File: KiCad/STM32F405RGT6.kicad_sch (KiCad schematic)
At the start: 44 parts, among them IC1 FT232RQ-REEL, J1 USB_C_Receptacle_USB2.0, J2 USB_C_Receptacle_USB2.0, SW1 SW_SPST, U1 STM32F405RGTx, U2 AT24CS64-SSHM, Y1 25MHz

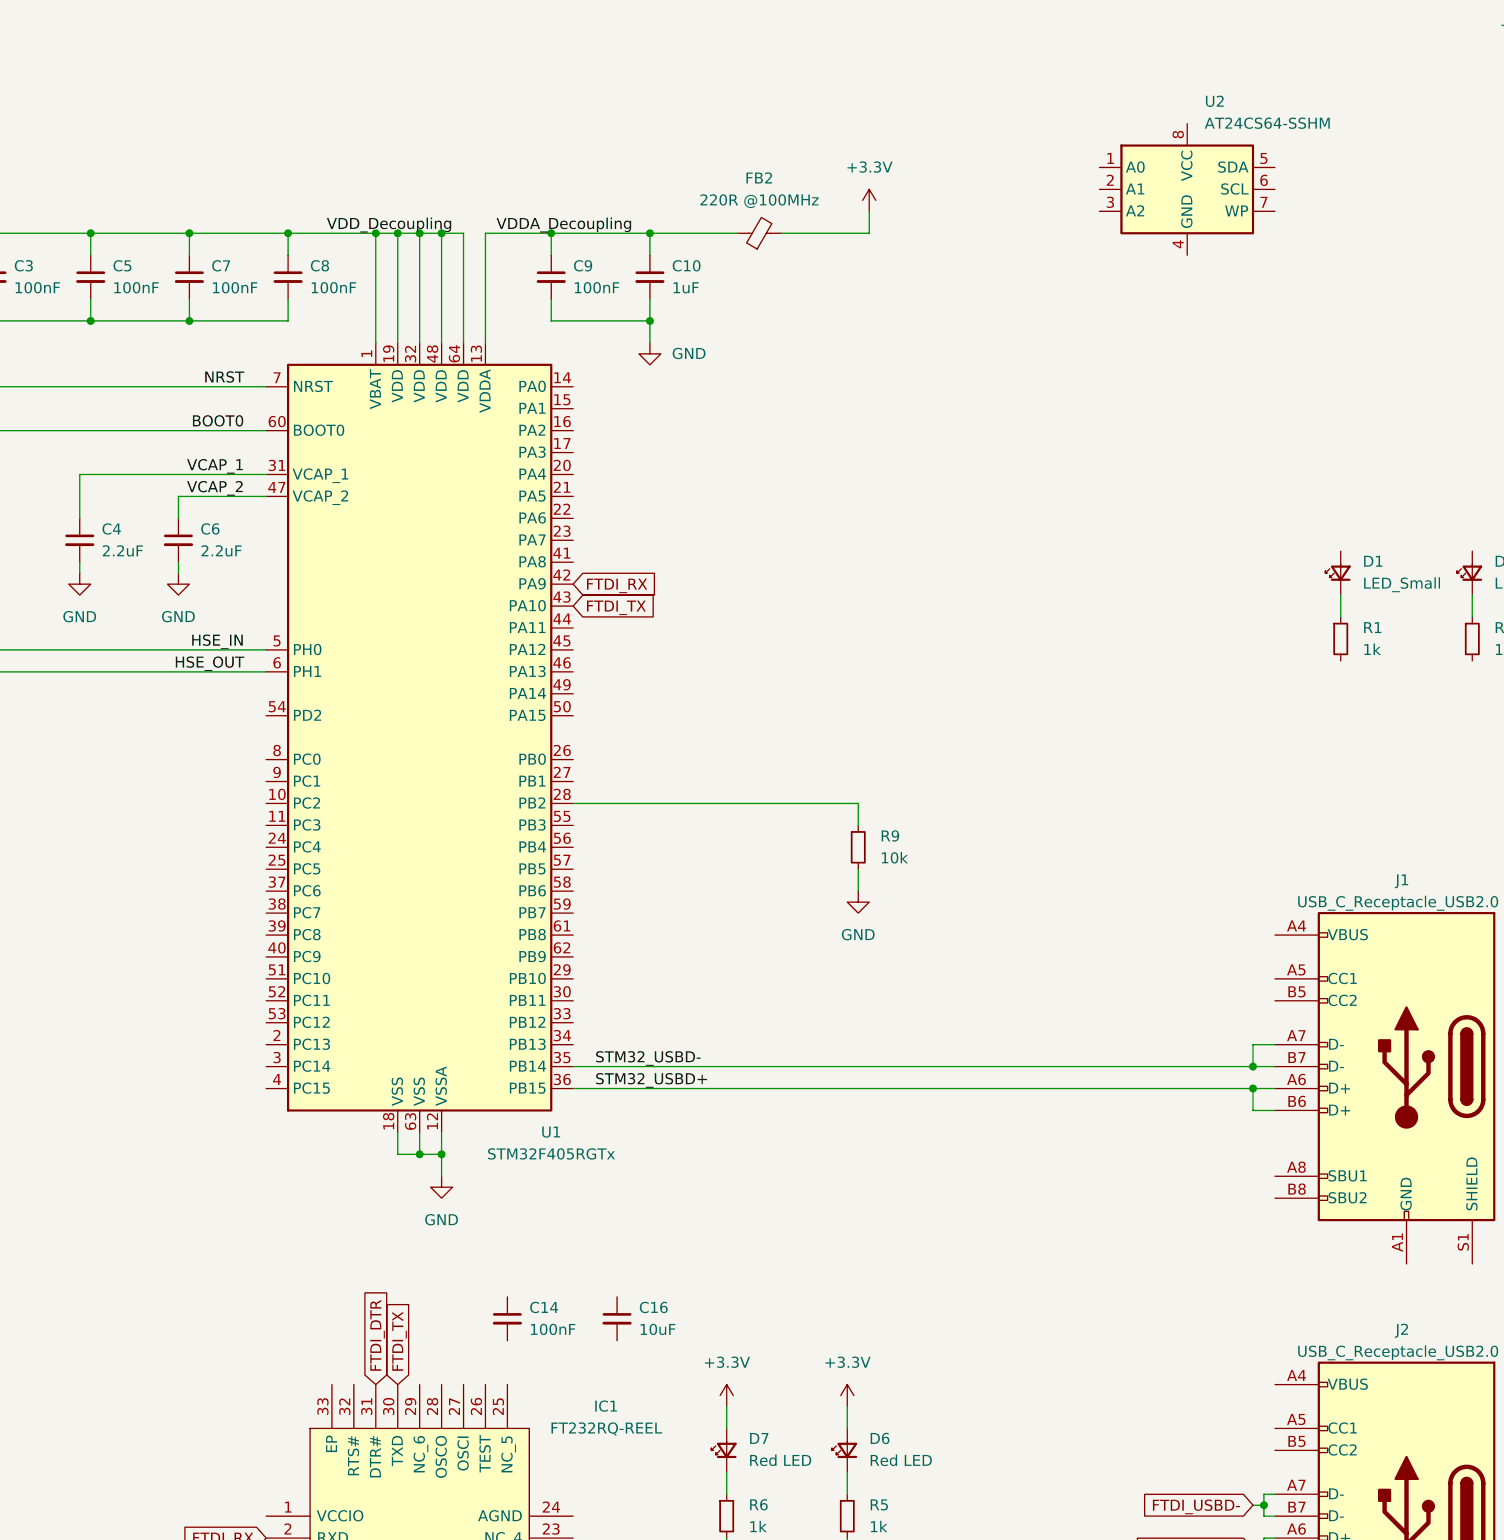
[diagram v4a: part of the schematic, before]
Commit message: Updated STM32 Cube and KiCad files
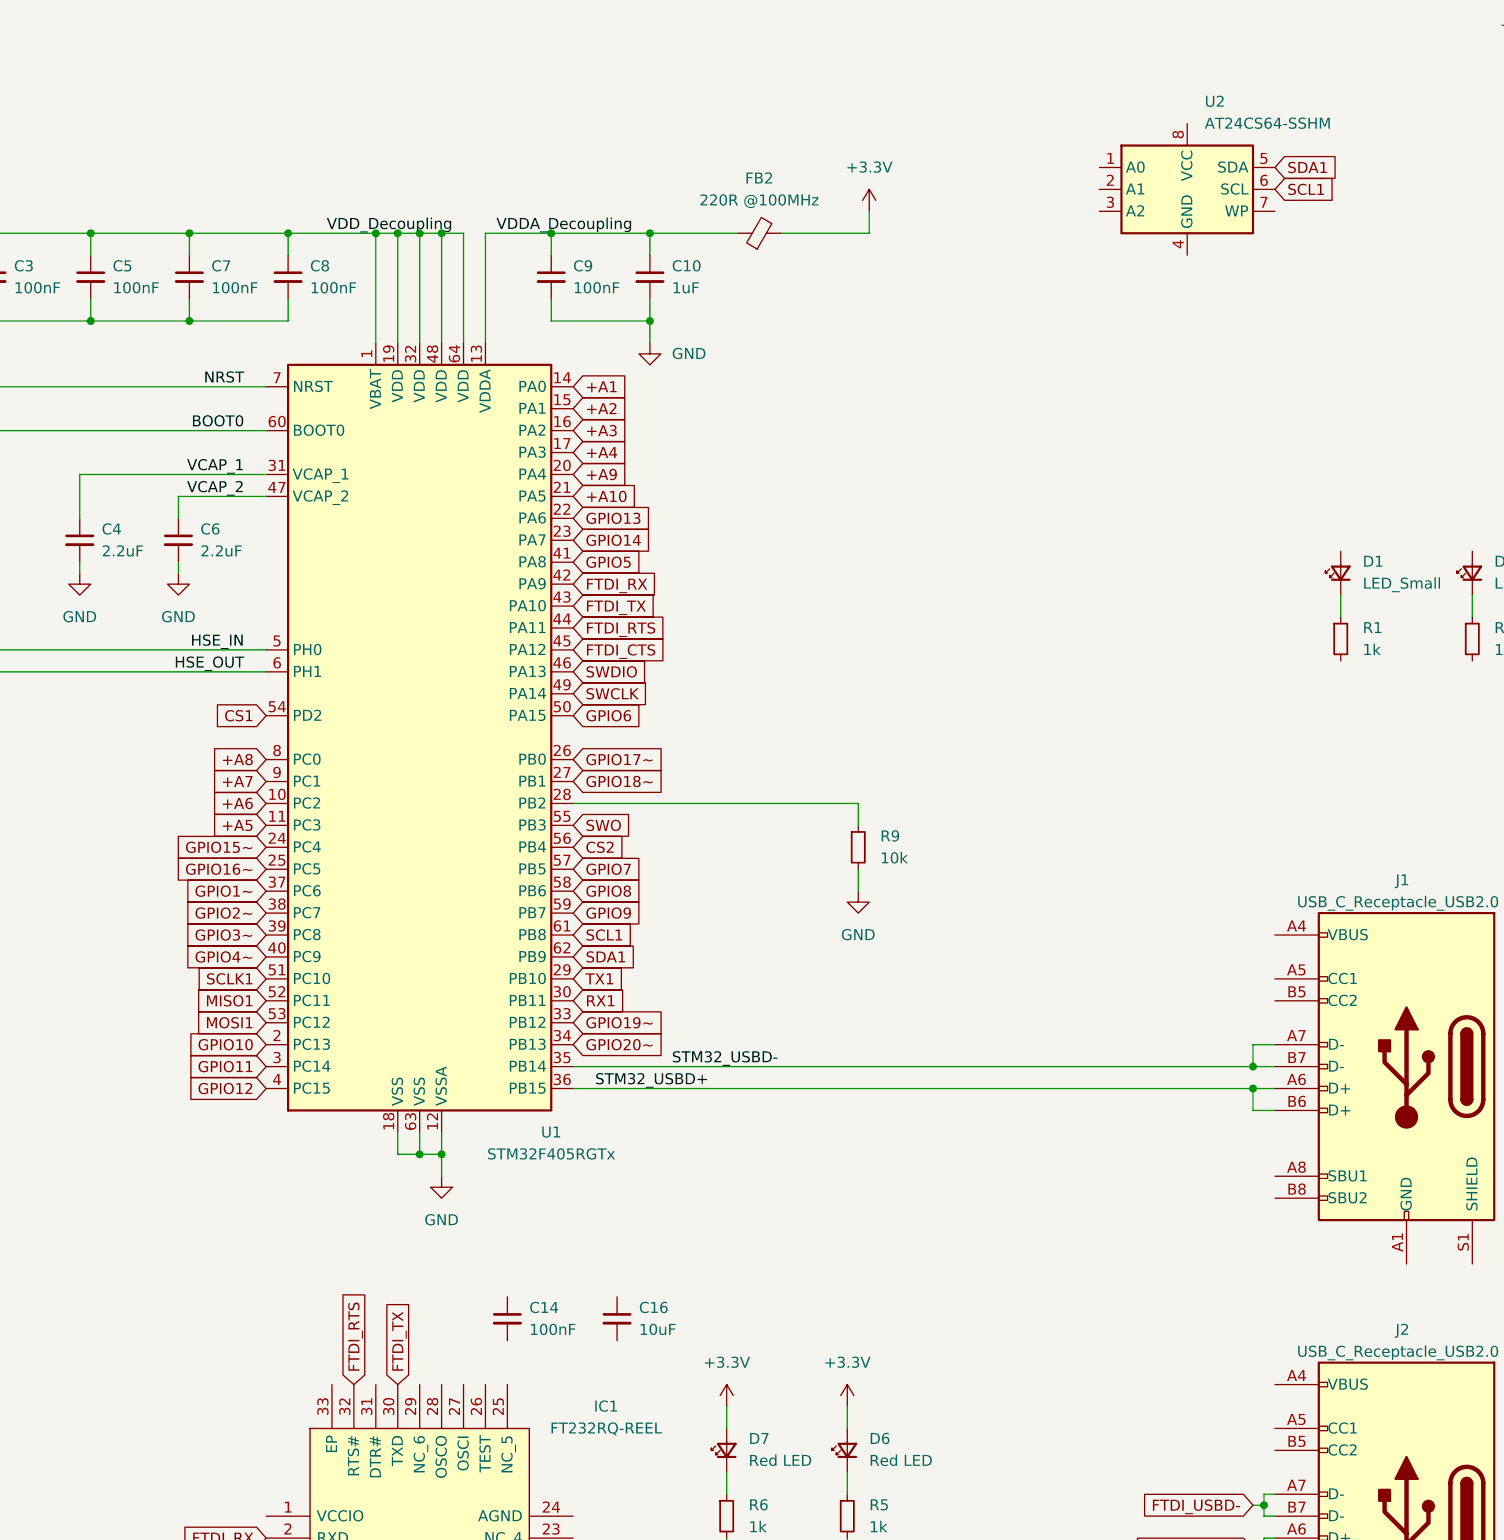
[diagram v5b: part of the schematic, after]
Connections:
- net FTDI_CTS: now also U1.45 (PA12)
- net FTDI_RTS: now reaches IC1.32 (RTS#)
- net FTDI_RTS: now also U1.44 (PA11)
- net +A6: now reaches U1.10 (PC2)
- net +A5: now reaches U1.11 (PC3)
- net +A1: now reaches U1.14 (PA0)
- net +A2: now reaches U1.15 (PA1)
- net +A3: now reaches U1.16 (PA2)
- net +A4: now reaches U1.17 (PA3)
- net GPIO10: now reaches U1.2 (PC13)
- net +A9: now reaches U1.20 (PA4)
- net +A10: now reaches U1.21 (PA5)
- net GPIO13: now reaches U1.22 (PA6)
- net GPIO14: now reaches U1.23 (PA7)
- net GPIO15~: now reaches U1.24 (PC4)
- net GPIO16~: now reaches U1.25 (PC5)
- net GPIO17~: now reaches U1.26 (PB0)
- net GPIO18~: now reaches U1.27 (PB1)
- net TX1: now reaches U1.29 (PB10)
- net GPIO11: now reaches U1.3 (PC14)
- net RX1: now reaches U1.30 (PB11)
- net GPIO19~: now reaches U1.33 (PB12)
- net GPIO20~: now reaches U1.34 (PB13)
- net GPIO1~: now reaches U1.37 (PC6)
- net GPIO2~: now reaches U1.38 (PC7)
- net GPIO3~: now reaches U1.39 (PC8)
- net GPIO12: now reaches U1.4 (PC15)
- net GPIO4~: now reaches U1.40 (PC9)
- net GPIO5: now reaches U1.41 (PA8)
- net SWDIO: now reaches U1.46 (PA13)
- net SWCLK: now reaches U1.49 (PA14)
- net GPIO6: now reaches U1.50 (PA15)
- net SCLK1: now reaches U1.51 (PC10)
- net MISO1: now reaches U1.52 (PC11)
- net MOSI1: now reaches U1.53 (PC12)
- net CS1: now reaches U1.54 (PD2)
- net SWO: now reaches U1.55 (PB3)
- net CS2: now reaches U1.56 (PB4)
- net GPIO7: now reaches U1.57 (PB5)
- net GPIO8: now reaches U1.58 (PB6)
- net GPIO9: now reaches U1.59 (PB7)
- net SCL1: now reaches U1.61 (PB8)
- net SCL1: now also U2.6 (SCL)
- net SDA1: now reaches U1.62 (PB9)
- net SDA1: now also U2.5 (SDA)
- net +A8: now reaches U1.8 (PC0)
- net +A7: now reaches U1.9 (PC1)
- net FTDI_DTR: no longer names the net of IC1.31 (DTR#)

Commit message: Update Schematic and PCB
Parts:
- added D10, D9: PRTR5V0U2X, Package_TO_SOT_SMD:SOT-143, symbol Power_Protection:PRTR5V0U2X
- added FB3, FB4: 220R @100MHz, Inductor_SMD:L_0603_1608Metric, symbol Device:FerriteBead_Small
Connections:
- net FTDI_USBD+: now also D9.3 (I/O2)
- net FTDI_USBD-: now also D9.2 (I/O1)
- net GND: now also J1.A1 (GND), J1.A12 (GND), J1.B1 (GND), J1.B12 (GND), J2.A1 (GND), J2.A12 (GND), J2.B1 (GND), J2.B12 (GND), D10.1 (GND), D9.1 (GND)
- net STM32_USBD+: now also D10.3 (I/O2)
- net STM32_USBD-: now also D10.2 (I/O1)
- net at J1.A4 (VBUS), J1.A9 (VBUS), J1.B4 (VBUS)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: now also D10.4 (VCC), FB3.2
- net at J2.A4 (VBUS), J2.A9 (VBUS), J2.B4 (VBUS)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: now also D9.4 (VCC), FB4.2
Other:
- moved on the sheet: D1, D2, D3, D5, J2, R1, R2, R3, R4

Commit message: Updated PCB and Schematic
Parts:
- removed C14, C15: 100nF, Capacitor_SMD:C_0603_1608Metric, symbol Device:C_Small
- removed C16: 10uF, Capacitor_SMD:C_0603_1608Metric, symbol Device:C_Small
- removed D6, D7: Red LED, LED_SMD:LED_0603_1608Metric, symbol Device:LED_Small
- removed D9: PRTR5V0U2X, Package_TO_SOT_SMD:SOT-143, symbol Power_Protection:PRTR5V0U2X
- removed FB4: 220R @100MHz, Inductor_SMD:L_0603_1608Metric, symbol Device:FerriteBead_Small
- removed IC1: FT232RQ-REEL, Package_DFN_QFN:QFN-32-1EP_5x5mm_P0.5mm_EP3.3x3.3mm_ThermalVias, symbol FT232RQ-REEL:FT232RQ-REEL
- removed J2: USB_C_Receptacle_USB2.0, Connector_USB:USB_C_Receptacle_HRO_TYPE-C-31-M-12, symbol Connector:USB_C_Receptacle_USB2.0
- removed R5, R6: 1k, Resistor_SMD:R_0603_1608Metric, symbol Device:R_Small
- added D6: D_Small, symbol Device:D_Small
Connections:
- net +5V: now also D6.1 (K)
- net USB_5V: now reaches D10.4 (VCC), FB3.2, J1.A4 (VBUS), J1.A9 (VBUS), J1.B4 (VBUS), J1.B9 (VBUS)
- net at FB3.1: now also D6.2 (A)
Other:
- note added: "90 Ohm differential pair for USB PCB Type: Trace Width: Trace Spacing: 1.6 mm, 4 layer board"
- moved on the sheet: D10, FB3, J1

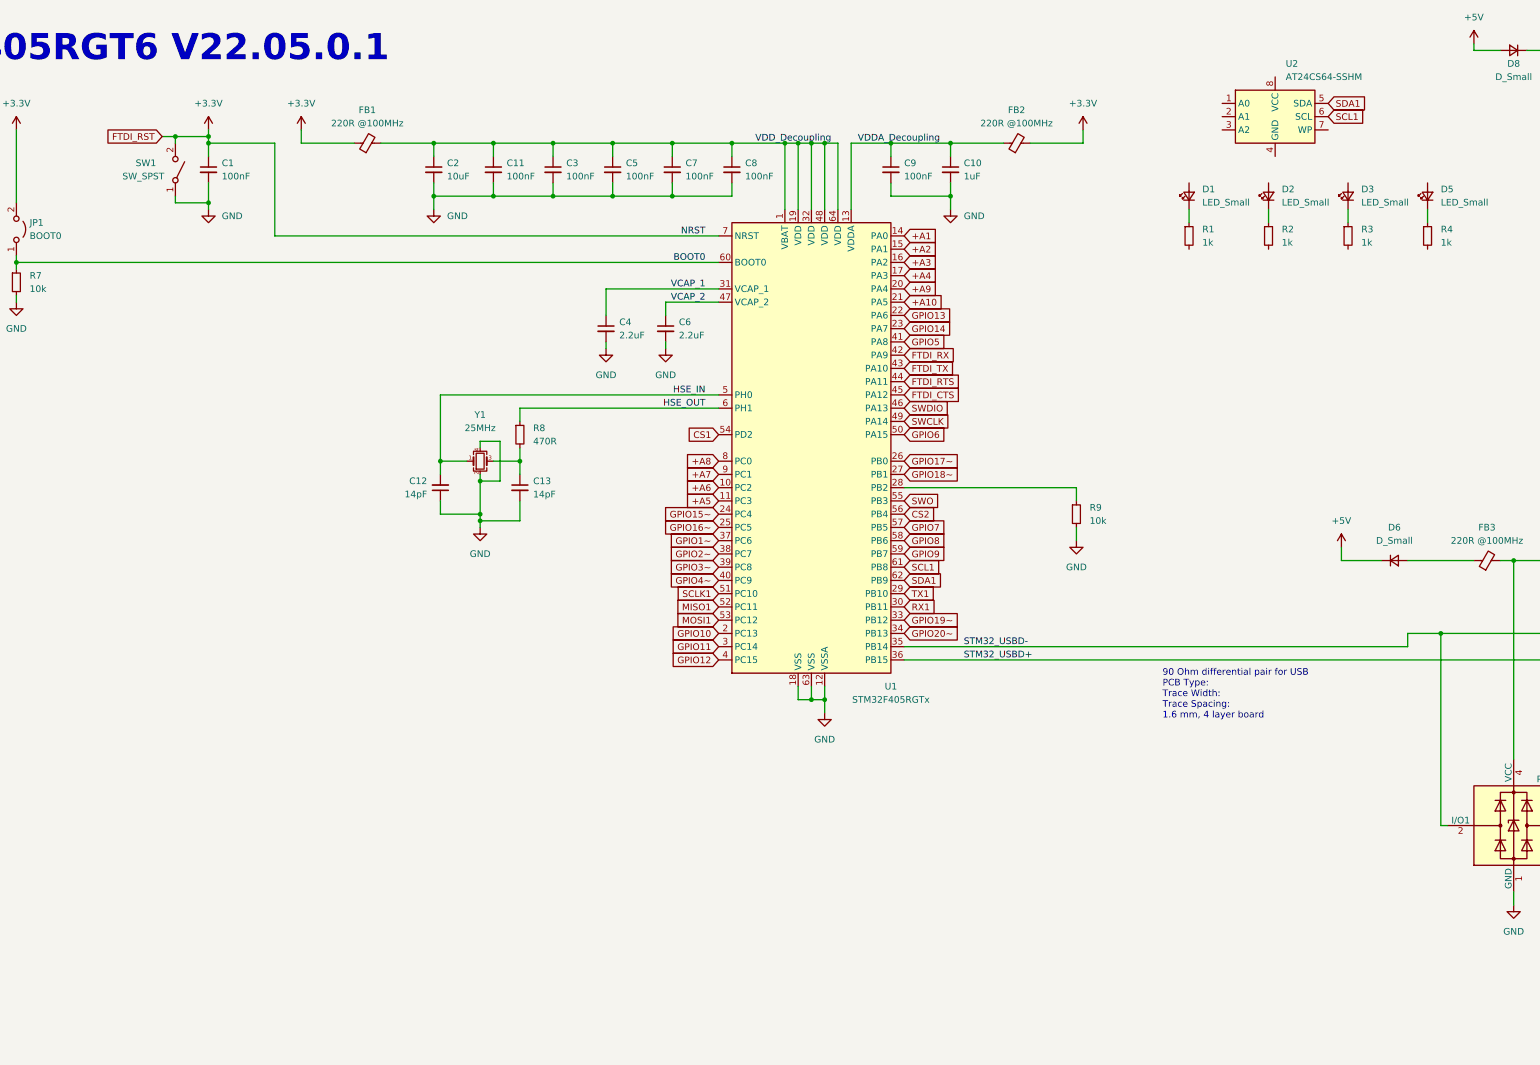
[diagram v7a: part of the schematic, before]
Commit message: Removed FTDI chip and rearranged pinout
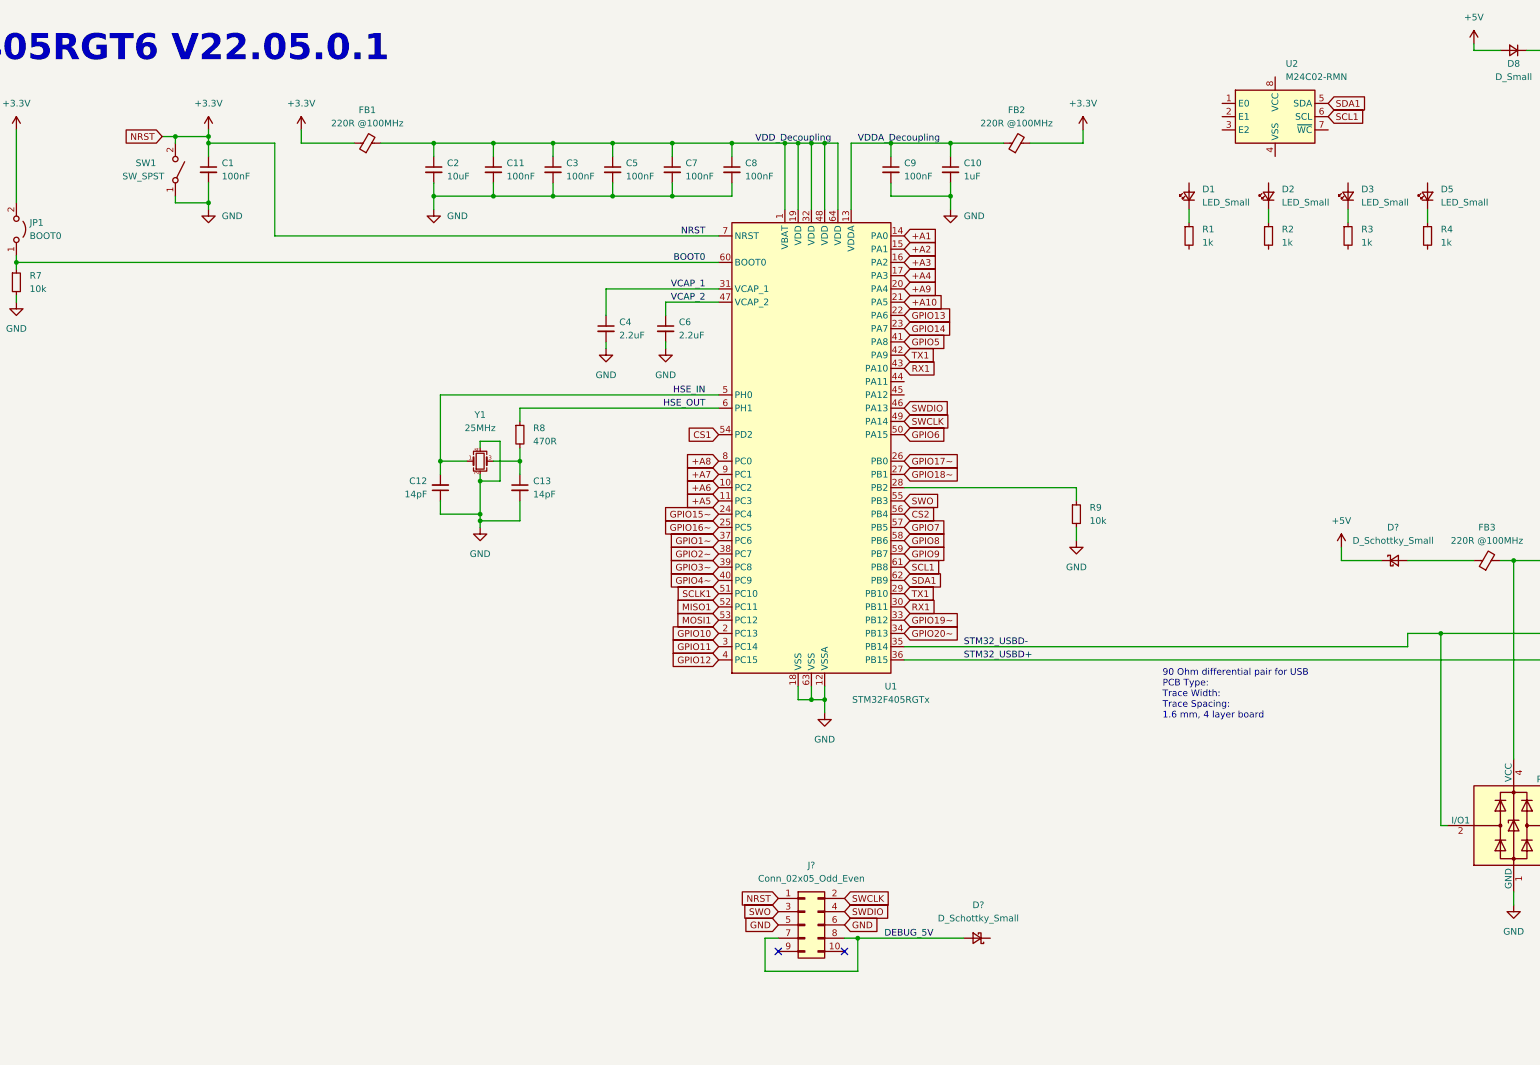
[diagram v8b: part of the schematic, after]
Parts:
- removed D6: D_Small, symbol Device:D_Small
- removed U2: AT24CS64-SSHM, Package_SO:SOIC-8_3.9x4.9mm_P1.27mm, symbol Memory_EEPROM:AT24CS64-SSHM
- added D? (x2): D_Schottky_Small, symbol Device:D_Schottky_Small
- added J?: Conn_02x05_Odd_Even, symbol Connector_Generic:Conn_02x05_Odd_Even
- added U2: M24C02-RMN, Package_SO:SOIC-8_3.9x4.9mm_P1.27mm, symbol Memory_EEPROM:M24C02-RMN
- D4: JLCPCB Part # (none) -> C2761795; Mouser Part Number 474-COM-16346 -> (none); Part Number COM-16346 -> WS2812B-B/W
- FB1, FB2, FB3: JLCPCB Part # (none) -> C88980; Mouser Part Number 810-MMZ1608Y221BTA00 -> 81-BLM18KG221SN1D; Part Number MMZ1608Y221BTA00 -> BLM18KG221SN1D
- J1: footprint Connector_USB:USB_C_Receptacle_HRO_TYPE-C-31-M-12 -> https://datasheet.lcsc.com/lcsc/2205251630_Korean-Hroparts-Elec-TYPE-C-31-M-12_C165948.pdf; JLCPCB Part # (none) -> C165948; Part Number (none) -> TYPE-C-31-M-12
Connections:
- net FTDI_RX is gone; now on net TX1: U1.42 (PA9)
- net FTDI_TX is gone; now on net RX1: U1.43 (PA10)
- net +3V3: now also J?.1 (Pin_1)
- net +5V: now also D?.1 (K)
- net GND: now also J?.5 (Pin_5), J?.6 (Pin_6)
- net SCL1: now also U2.6 (SCL)
- net SDA1: now also U2.5 (SDA)
- net SWCLK: now also J?.2 (Pin_2)
- net SWDIO: now also J?.4 (Pin_4)
- net SWO: now also J?.3 (Pin_3)
- net at FB3.1: now also D?.2 (A)
- net FTDI_CTS: no longer names the net of U1.45 (PA12)
- net FTDI_RTS: no longer names the net of U1.44 (PA11)
- new net DEBUG_5V: D?.2 (A), J?.7 (Pin_7), J?.8 (Pin_8)
- no-connect marks 1 -> 3
